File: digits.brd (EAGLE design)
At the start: 240.9 x 79 mm, 48 parts, among them IC1 STP16CP05 / STP16CPC26, IC2 STP16CP05 / STP16CPC26, IC3 ATMEGA32U4QFN, IC4 ATMEGA32U4TQFP-44, J1 POWER_JACKPTH_LOCK, J2 ACCESSORY, X1 CRYSTALHC49

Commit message: layout
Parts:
- JP4: value Bluefruit LE -> Adafruit Bluefruit LE
- moved JP4 22.9 mm to (82.0, 30.0), turned to 90 degrees
- moved JP5 22.8 mm to (120.0, 30.0), turned to 90 degrees
- moved SJ2 4.05 mm to (80.2, 44.1), turned to 270 degrees
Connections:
- net PD0: now also J2.11; no longer J2.9
- net PD1: now also J2.9; no longer J2.11
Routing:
- net PD1: track 267.9 -> 103.1 mm, vias 4 -> 2
- net SCK: track 321.3 -> 230.5 mm, vias 10 -> 9
- net MOSI: track 262.9 -> 180.9 mm, vias 10 -> 9
- net VCC: track 665.9 -> 610.3 mm
- net PD7: track 104.2 -> 53.2 mm
- net PB4: track 105.6 -> 55.2 mm
- net MISO: track 186.1 -> 135.7 mm
- net ROW1: track 94.8 -> 51.9 mm, vias 3 -> 2
- net PD0: track 268.8 -> 235.8 mm
- net BF_RDY: track 27.4 -> 0.00 mm, vias 1 -> 0
- net WIFI_IRQ: track 59.3 -> 45.2 mm
- net PC7: track 58.6 -> 67.5 mm
- net PD6: track 70.0 -> 72.8 mm, vias 3 -> 4
- net PB7: track 125.2 -> 126.4 mm, vias 4 -> 5
- net VCCIC: track 81.7 -> 82.3 mm
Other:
- board text added: "3Vo"
- board text added: "3v3"
- board text added: "5V"
- board text added: "A0"
- board text added: "A1"
- board text added: "A2"
- board text added: "A4"
- board text added: "A5"
- board text added: "ACT"
- board text added: "BLANK"
- board text added: "CLK"
- board text added: "CS"
- board text added: "D0"
- board text added: "D1"
- board text added: "D11"
- board text added: "D12"
- board text added: "D13"
- board text added: "D14"
- board text added: "D15"
- board text added: "D16"
- board text added: "D17"
- board text added: "D2"
- board text added: "D3"
- board text added: "D6"
- board text added: "D7"
- board text added: "D8"
- board text added: "GND"
- board text added: "IRQ"
- board text added: "LATCH"
- board text added: "MISO"
- board text added: "MOSI"
- board text added: "PREZ"
- board text added: "RDY"
- board text added: "REQ"
- board text added: "RST"
- board text added: "RX"
- board text added: "SCK"
- board text added: "SCL"
- board text added: "SDA"
- board text added: "TX"
- board text added: "VBEN"
- board text added: "VIN"

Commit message: more layout
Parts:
- moved SJ2 4.15 mm to (79.1, 40.1), turned to 180 degrees
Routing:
- net PD1: track 103.1 -> 262.2 mm, vias 2 -> 5
- net SCK: track 230.5 -> 311.0 mm
- net MOSI: track 180.9 -> 254.6 mm, vias 9 -> 10
- net PD7: track 53.2 -> 101.3 mm
- net PB4: track 55.2 -> 101.1 mm, vias 2 -> 3
- net ROW1: track 51.9 -> 96.3 mm, vias 2 -> 3
- net BF_RDY: track 0.00 -> 42.2 mm, vias 0 -> 3
- net MISO: track 135.7 -> 173.1 mm
- net WIFI_IRQ: track 45.2 -> 80.1 mm
- net VCC: track 610.3 -> 644.1 mm, vias 8 -> 10
- net PD0: track 235.8 -> 267.7 mm, vias 7 -> 9

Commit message: layout, added diode
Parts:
- added D2: (no value), SparkFun-DiscreteSemi:SOD-323
- D1: value DIODESOD-123F -> (none); device digits:SOD-123F -> SparkFun-DiscreteSemi:SOD-323
- moved J1 2.82 mm to (1.30, 57.2)
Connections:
- new net N$6: D2.A, J1.PWR
- net VCC: now also D2.C; no longer J1.PWR
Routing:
- net VCC: track 644.1 -> 631.2 mm
- net N$6: track 0.00 -> 12.5 mm
- net BLANK: track 337.4 -> 347.1 mm
- net MOSI: track 254.6 -> 246.4 mm
- net LATCH: track 305.5 -> 306.4 mm, vias 6 -> 8
- net PB7: track 126.4 -> 127.1 mm
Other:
- board text added: "2014 PloverElectric.com"
- board text added: "Digits"
- board text added: "Plover Electric"
- board text added: "Rev 0.1 July 12 2014"

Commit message: added more room for screw holes and 0.1 release
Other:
- board size 240.9 x 79 mm -> 240.9 x 81 mm
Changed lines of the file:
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@@
 <setting verticaltext="up"/>
 </settings>
-<grid distance="0.0999999999" unitdist="mm" unit="mm" style="lines" multiple="1" display="no" altdistance="0.025" altunitdist="inch" altunit="inch"/>
+<grid distance="0.1" unitdist="mm" unit="mm" style="lines" multiple="1" display="no" altdistance="0.025" altunitdist="inch" altunit="inch"/>
 <layers>
 <layer number="1" name="Top" color="4" fill="1" visible="yes" active="yes"/>
@@
 <layer number="42" name="bRestrict" color="1" fill="10" visible="yes" active="yes"/>
 <layer number="43" name="vRestrict" color="2" fill="10" visible="yes" active="yes"/>
-<layer number="44" name="Drills" color="7" fill="1" visible="no" active="yes"/>
-<layer number="45" name="Holes" color="7" fill="1" visible="no" active="yes"/>
+<layer number="44" name="Drills" color="7" fill="1" visible="yes" active="yes"/>
+<layer number="45" name="Holes" color="7" fill="1" visible="yes" active="yes"/>
 <layer number="46" name="Milling" color="3" fill="1" visible="yes" active="yes"/>
 <layer number="47" name="Measures" color="7" fill="1" visible="yes" active="yes"/>
@@
 <board>
 <plain>
-<wire x1="0.2" y1="-4" x2="241.1" y2="-4" width="0" layer="20"/>
-<wire x1="241.1" y1="-4" x2="241.1" y2="75" width="0" layer="20"/>
-<wire x1="241.1" y1="75" x2="0.2" y2="75" width="0" layer="20"/>
-<wire x1="0.2" y1="75" x2="0.2" y2="-4" width="0" layer="20"/>
-<hole x="3" y="72.75" drill="3"/>
-<hole x="238.1" y="72.75" drill="3"/>
-<hole x="238.1" y="-1.75" drill="3"/>
-<hole x="3" y="-1.75" drill="3"/>
+<wire x1="0.2" y1="-5" x2="241.1" y2="-5" width="0" layer="20"/>
+<wire x1="241.1" y1="-5" x2="241.1" y2="76" width="0" layer="20"/>
+<wire x1="241.1" y1="76" x2="0.2" y2="76" width="0" layer="20"/>
+<wire x1="0.2" y1="76" x2="0.2" y2="-5" width="0" layer="20"/>
+<hole x="4" y="73.25" drill="3"/>
+<hole x="237.1" y="73.25" drill="3"/>
+<hole x="237.1" y="-2.25" drill="3"/>
+<hole x="4" y="-2.25" drill="3"/>
 <text x="64" y="52.3" size="1.016" layer="22" rot="MR0">5V</text>
 <text x="64" y="49.76" size="1.016" layer="22" rot="MR0">GND</text>
@@
 <contactref element="JP3" pad="1"/>
 <contactref element="SJ4" pad="2"/>
-<wire x1="9.1" y1="-2.5" x2="56.8" y2="-2.5" width="2.1844" layer="16"/>
+<wire x1="9.7" y1="-2.5" x2="56.8" y2="-2.5" width="2.1844" layer="16"/>
 <wire x1="56.8" y1="-2.5" x2="86.9" y2="-2.5" width="2.1844" layer="16"/>
 <wire x1="86.9" y1="-2.5" x2="105.5" y2="-2.5" width="2.1844" layer="16"/>
@@
 <wire x1="57.0746" y1="3.384" x2="57.0746" y2="-2.2254" width="0.6096" layer="16"/>
 <wire x1="57.0746" y1="-2.2254" x2="56.8" y2="-2.5" width="0.6096" layer="16"/>
-<wire x1="9.3746" y1="-2.2254" x2="9.1" y2="-2.5" width="0.6096" layer="16"/>
+<wire x1="9.3746" y1="-2.2254" x2="9.7" y2="-2.5" width="0.6096" layer="16"/>
 <wire x1="8.27" y1="42.58" x2="5.73" y2="42.58" width="2.1844" layer="16"/>
 <wire x1="5.73" y1="42.58" x2="2.32" y2="42.58" width="2.1844" layer="16"/>
@@
 <wire x1="87.1" y1="-2.3" x2="87.05" y2="-2.35" width="0.6096" layer="16"/>
 <wire x1="87.05" y1="-2.35" x2="86.9" y2="-2.5" width="0.6096" layer="16"/>
-<wire x1="9.1" y1="-2.5" x2="6.8" y2="-0.2" width="2.1844" layer="16" curve="-90"/>
-<wire x1="6.8" y1="-0.2" x2="6.8" y2="-0.1" width="2.1844" layer="16"/>
-<wire x1="6.8" y1="-0.1" x2="5.2" y2="2" width="2.1844" layer="16" curve="90"/>
-<wire x1="5.2" y1="2" x2="4" y2="2" width="2.1844" layer="16"/>
+<wire x1="9.7" y1="-2.5" x2="7.4" y2="-0.2" width="2.1844" layer="16" curve="-90"/>
+<wire x1="7.4" y1="-0.2" x2="7.4" y2="-0.1" width="2.1844" layer="16"/>
+<wire x1="7.4" y1="-0.1" x2="5.8" y2="2" width="2.1844" layer="16" curve="90"/>
+<wire x1="5.8" y1="2" x2="4" y2="2" width="2.1844" layer="16"/>
 <wire x1="4" y1="2" x2="2.1" y2="3.4" width="2.1844" layer="16" curve="-90"/>
 <wire x1="2.1" y1="3.4" x2="2.1" y2="9.7" width="2.1844" layer="16"/>
@@
 <wire x1="7.3906" y1="1.4" x2="7.3" y2="1.4" width="0.6096" layer="16"/>
 <wire x1="7.3" y1="1.4" x2="6.8" y2="0.9" width="0.6096" layer="16" curve="90"/>
-<wire x1="6.8" y1="0.9" x2="6.8" y2="-0.1" width="0.6096" layer="16"/>
+<wire x1="6.8" y1="0.9" x2="7.4" y2="-0.1" width="0.6096" layer="16"/>
 <wire x1="5.25" y1="9.7" x2="2.1" y2="9.7" width="1.27" layer="16"/>
 <wire x1="163.65" y1="42.08" x2="161.78" y2="42.08" width="0.3048" layer="16"/>

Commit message: finished BOM
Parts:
- D1, D2: value (none) -> PMEG3030EP; device SparkFun-DiscreteSemi:SOD-323 -> digits:SOD-128
- J2: device digits:2X16 -> digits:2X13
- moved D2 0.60 mm to (5.10, 50.1), turned to 0 degrees
- moved D1 0.20 mm to (6.60, 9.70), turned to 0 degrees
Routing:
- net N$6: track 12.5 -> 10.8 mm
- net VCC: track 631.4 -> 630.1 mm
- net N$3: track 12.2 -> 11.0 mm

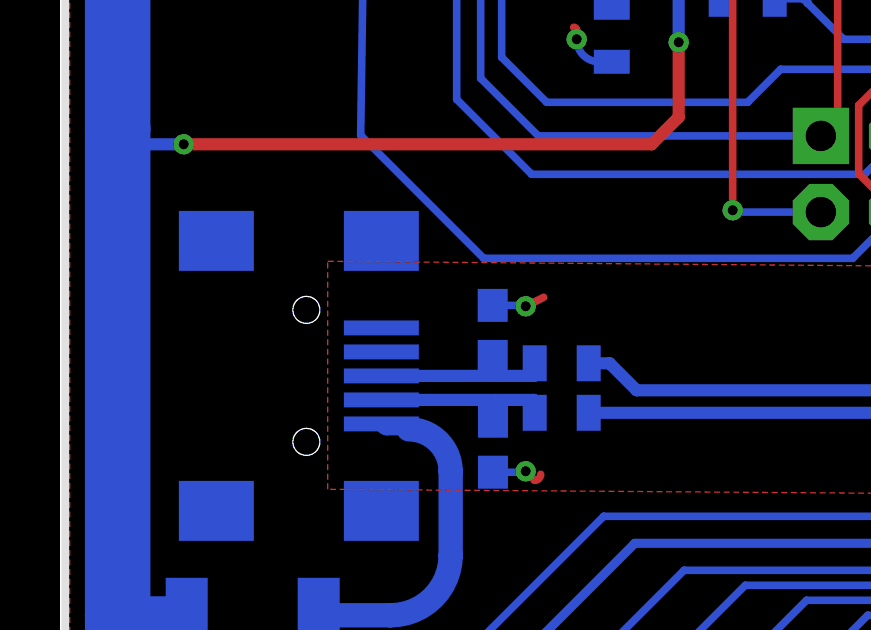
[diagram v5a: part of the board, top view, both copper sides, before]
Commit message: grounded usb (fixes #3)
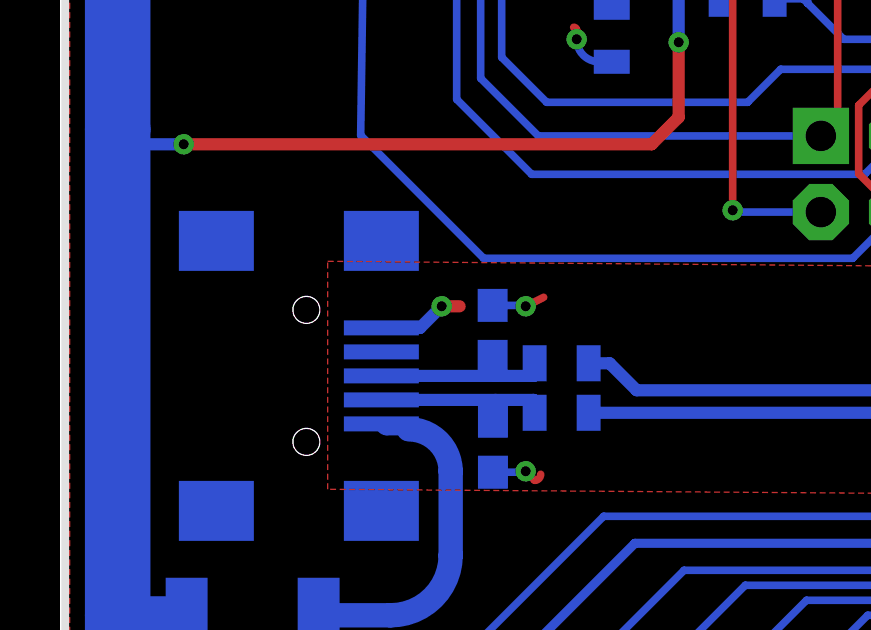
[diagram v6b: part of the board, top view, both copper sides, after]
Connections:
- net GND: now also JP2.GND
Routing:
- net GND: track 56.6 -> 59.5 mm, vias 19 -> 20
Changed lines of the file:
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@@
 <wire x1="27.8" y1="37.2" x2="27.75" y2="37.15" width="0.254" layer="16"/>
 <wire x1="27.75" y1="37.15" x2="27.05" y2="37.15" width="0.254" layer="16"/>
+<contactref element="JP2" pad="GND"/>
+<wire x1="10.89" y1="19.28" x2="12.18" y2="19.28" width="0.4064" layer="16"/>
+<wire x1="12.18" y1="19.28" x2="12.9" y2="20" width="0.4064" layer="16"/>
+<via x="12.9" y="20" extent="1-16" drill="0.3302"/>
+<wire x1="12.9" y1="20" x2="13.5" y2="20" width="0.4064" layer="1"/>
 </signal>
 <signal name="N$1">

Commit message: increased screw hole size, added resistors, fixed mosfets (fixes #4 fixes #7 fixes #6)
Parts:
- added R10, R11, R12, R7, R9: 1k, SparkFun-Resistors:0805
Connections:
- new net N$10: R9.2, T2.3
- new net N$11: R10.2, T3.3
- new net N$12: R12.2, T5.3
- new net N$8: R11.2, T4.3
- new net N$9: R7.2, T1.3
- net GATE0: now also R7.1; no longer T1.3
- net GATE1: now also R9.1; no longer T2.3
- net GATE2: now also R10.1; no longer T3.3
- net GATE3: now also R11.1; no longer T4.3
- net GATE4: now also R12.1; no longer T5.3
- net ROW0: now also T1.1; no longer T1.2
- net ROW1: now also T2.1; no longer T2.2
- net ROW2: now also T3.1; no longer T3.2
- net ROW3: now also T4.1; no longer T4.2
- net ROW4: now also T5.1; no longer T5.2
- net VCC: now also T1.2, T2.2, T3.2, T4.2, T5.2; no longer T1.1, T2.1, T3.1, T4.1, T5.1
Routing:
- net VCC: track 630.1 -> 604.2 mm
- net GATE0: track 77.7 -> 74.8 mm
- net GATE3: track 164.6 -> 163.3 mm
- net GATE4: track 201.1 -> 200.0 mm
- net GATE1: track 66.2 -> 65.2 mm

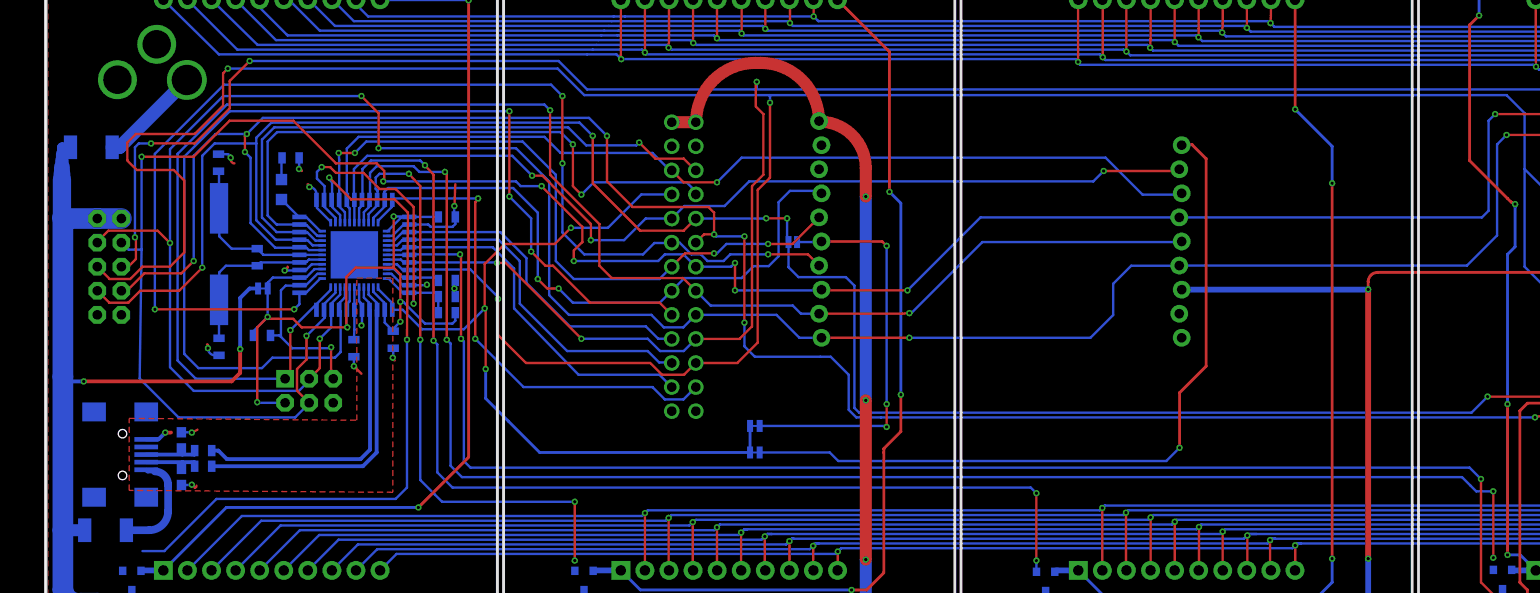
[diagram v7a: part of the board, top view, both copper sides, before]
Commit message: removed adafruit headers, added spark core, reassigning acc pins, reassigning power buses
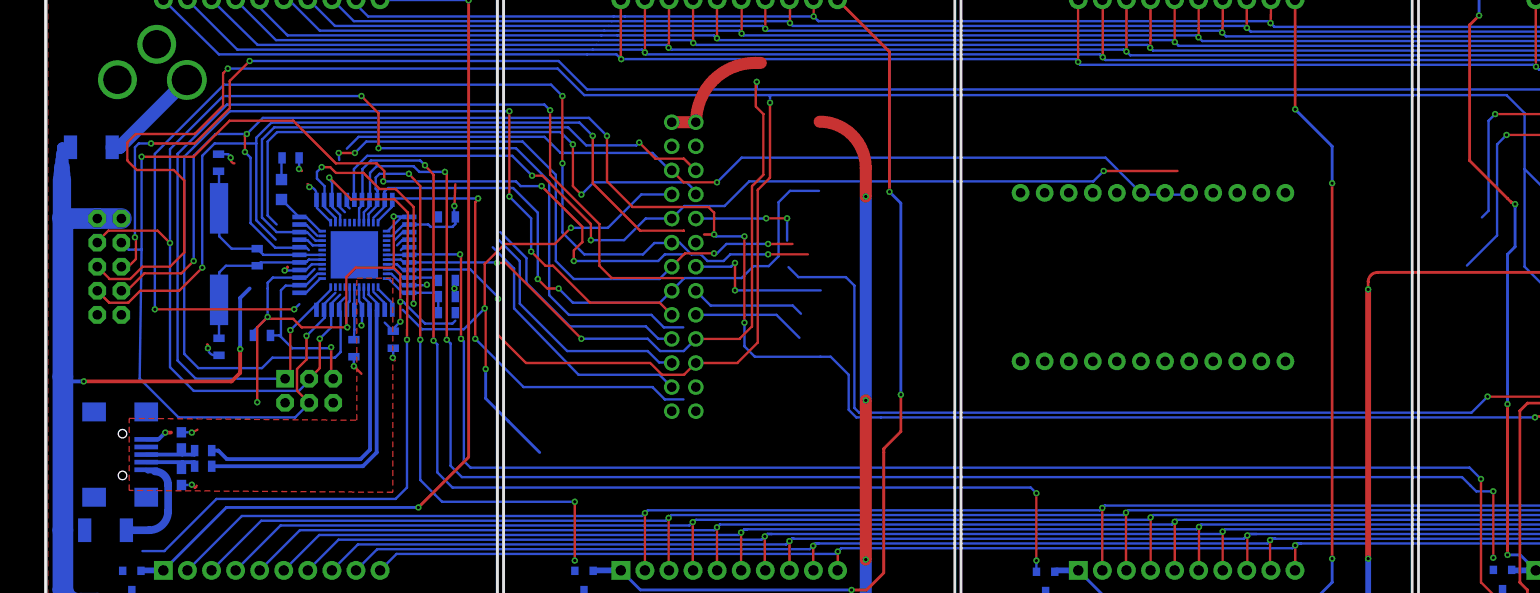
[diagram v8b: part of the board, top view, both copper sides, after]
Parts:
- removed JP4: Adafruit Bluefruit LE, SparkFun-Connectors:1X10_LOCK
- removed JP5: Adafruit CC3000 Wifi, SparkFun-Connectors:1X09_LOCK
- removed SJ1, SJ3: SOLDERJUMPERTRACE, SparkFun-Passives:SJ_2S-TRACE
- removed SJ2: SOLDERJUMPERNO, SparkFun-Passives:SJ_2S-NO
- removed SJ4: SOLDERJUMPERTRACE, SparkFun-Retired:SJ_2S-TRACE
- added U$1: SPARK_CORECORE, Spark:SPARK_CORE
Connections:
- removed net BF_RDY: JP4.5, SJ1.2, SJ2.2
- removed net MISO: IC3.11, IC4.11, J2.15, JP1.1, JP4.2, JP5.5
- removed net PB0: IC3.8, IC4.8, J2.18
- removed net PB4: IC3.28, IC4.28, J2.10, JP5.8
- removed net PB7: IC3.12, IC4.12, J2.12, JP4.4
- removed net PC7: IC3.32, IC4.32, J2.16, JP4.7
- removed net PD2: IC3.20, IC4.20, J2.5
- removed net PD3: IC3.21, IC4.21, J2.7
- removed net PD6: IC3.26, IC4.26, J2.14, JP4.6
- removed net PD7: IC3.27, IC4.27, J2.6, JP5.7
- removed net PE6: IC3.1, IC4.1, J2.8, SJ1.1, SJ3.1
- removed net PF5: IC3.38, IC4.38, J2.24
- removed net PF6: IC3.37, IC4.37, J2.22
- removed net PF7: IC3.36, IC4.36, J2.20
- removed net PRESENCE: IC3.33, IC4.33, J2.23
- removed net VCCIC: C8.1, C9.1, IC3.14, IC3.2, IC3.34, IC3.7, IC4.14, IC4.2, IC4.34, IC4.7, JP1.2, L1.1, R6.2, SJ4.1
- removed net WIFI_IRQ: JP5.9, SJ3.2
- new net A0: IC3.36, IC4.36, J2.20, U$1.12
- new net A1: IC3.37, IC4.37, J2.22, U$1.11
- new net A2: IC3.38, IC4.38, J2.24, U$1.10
- new net D0/RX: J2.5, U$1.4
- new net D1/TX: J2.7, U$1.3
- new net D10: IC3.26, IC4.26, J2.12
- new net D11: IC3.32, IC4.32, J2.14
- new net D12: IC3.8, IC4.8, J2.16
- new net D13: J2.18
- new net D2/SDA: IC3.19, IC4.19, J2.9, U$1.13
- new net D3/SCL: IC3.18, IC4.18, J2.11, U$1.14
- new net D4/MOSI: IC3.10, IC4.10, J2.13, JP1.4, U$1.7
- new net D5/MISO: IC3.11, IC4.11, J2.15, JP1.1, U$1.8
- new net D6: IC3.27, IC4.27
- new net D6/SCK: IC3.9, IC4.9, J2.17, JP1.3, U$1.9
- new net D7: IC3.1, IC4.1, J2.6
- new net D7/PRESENCE: IC3.33, IC4.33, J2.23, U$1.20
- new net D8: IC3.28, IC4.28, J2.8
- new net D9: IC3.12, IC4.12, J2.10
- new net RX: IC3.20, IC4.20
- new net TX: IC3.21, IC4.21
- new net VCC5V: C8.1, C9.1, D1.C, IC3.14, IC3.2, IC3.34, IC3.7, IC4.14, IC4.2, IC4.34, IC4.7, JP1.2, L1.1, R6.2, U$1.1
- new net VCC9V: D2.C
- new net VDDA: U$1.22
- net BLANK: now also U$1.6
- net GATE0: now also U$1.15
- net GATE1: now also U$1.16
- net GATE2: now also U$1.17
- net GATE3: now also U$1.18
- net GATE4: now also U$1.19
- net GND: now also U$1.2, U$1.21; no longer JP4.9, JP5.1
- net LATCH: now also U$1.5
- net MOSI: no longer IC3.10, IC4.10, J2.13, JP1.4, JP4.3, JP5.6
- net PD0: no longer IC3.18, IC4.18, J2.11
- net PD1: no longer IC3.19, IC4.19, J2.9, SJ2.1
- net SCK: no longer IC3.9, IC4.9, J2.17, JP1.3, JP4.1, JP5.4
- net VCC: now also U$1.24; no longer D1.C, D2.C, JP4.10, JP5.3, SJ4.2
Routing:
- net MISO: track 173.1 -> 0.00 mm, vias 3 -> 0
- net D5/MISO: track 0.00 -> 127.5 mm, vias 0 -> 2
- net PB7: track 127.1 -> 0.00 mm, vias 5 -> 0
- net D10: track 0.00 -> 122.8 mm, vias 0 -> 5
- net PB0: track 115.4 -> 0.00 mm, vias 3 -> 0
- net D13: track 0.00 -> 112.6 mm, vias 0 -> 3
- net MOSI: track 246.4 -> 140.8 mm, vias 10 -> 6
- net PD7: track 101.3 -> 0.00 mm, vias 1 -> 0
- net D9: track 0.00 -> 101.2 mm, vias 0 -> 3
- net PB4: track 101.1 -> 0.00 mm, vias 3 -> 0
- net SCK: track 311.0 -> 210.4 mm, vias 9 -> 7
- net D7: track 0.00 -> 96.0 mm, vias 0 -> 1
- net PE6: track 84.6 -> 0.00 mm, vias 3 -> 0
- net VCCIC: track 82.3 -> 0.00 mm, vias 6 -> 0
- net WIFI_IRQ: track 80.1 -> 0.00 mm, vias 1 -> 0
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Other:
- board text removed: "3Vo"
- board text removed: "3v3"
- board text removed: "ACT"
- board text removed: "CLK"
- board text removed: "IRQ"
- board text removed: "REQ"
- board text removed: "RST"
- board text removed: "VBEN"
- board text removed: "VIN"
